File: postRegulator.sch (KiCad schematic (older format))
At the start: 18 parts

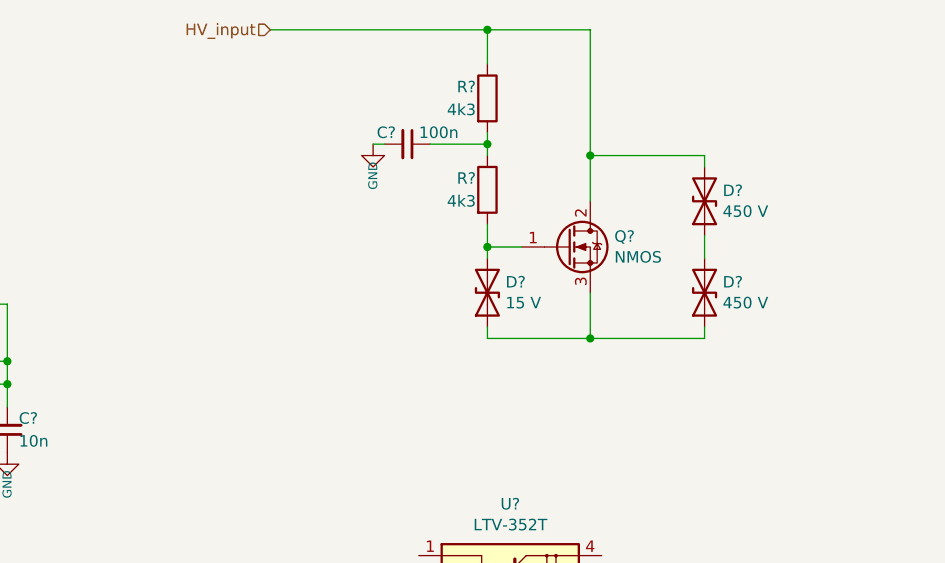
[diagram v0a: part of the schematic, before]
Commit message: - added DC/DC converter to library, - moved ammeter & drivers to sub-sheet, - further develop
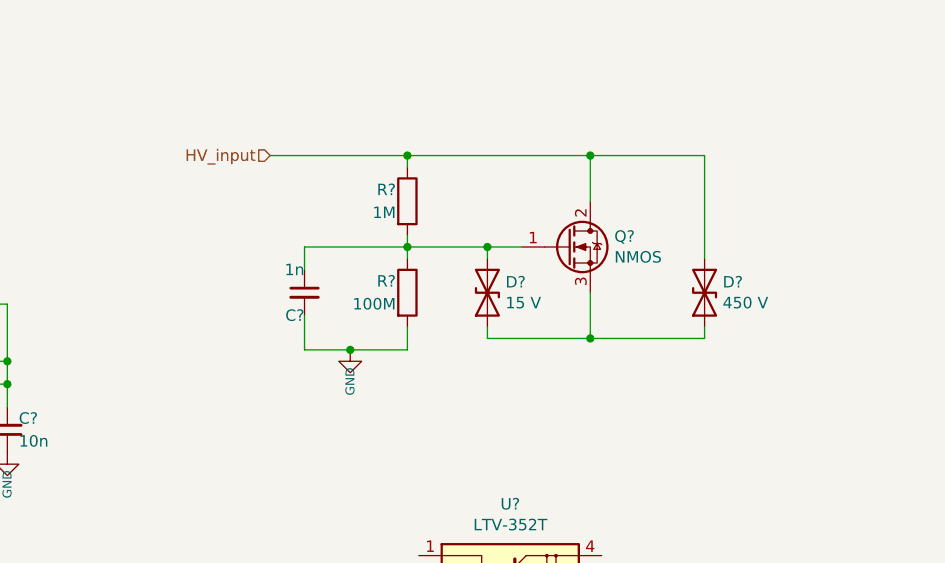
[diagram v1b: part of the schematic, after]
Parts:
- removed D?: 450 V, symbol Device:D_TVS
- C?: value 100n -> 1n
- R?: value 4k3 -> 100M
- R?: value 4k3 -> 1M
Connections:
- net GND: now also R?.2
- net at D?.2 (A2), Q?.1 (G): now also C?.1, R?.1, R?.2; no longer R?.2
- net at D?.1 (A1), Q?.3 (S): now also D?.1 (A1)
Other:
- moved on the sheet: C?, D?, R?
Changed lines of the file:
@@
 $Descr A4 11693 8268
 encoding utf-8
-Sheet 6 7
+Sheet 6 8
 Title ""
 Date ""
@@
 Wire Wire Line
 	3550 3700 3550 3650
-Text HLabel 2600 2350 0    50   Input ~ 0
+Text HLabel 2600 2900 0    50   Input ~ 0
 HV_input
-Wire Wire Line
-	2600 2350 3550 2350
-Wire Wire Line
-	4000 2350 4000 2900
 $Comp
 L Device:D_TVS D?
-U 1 1 5F4666BF
+U 1 1 5F466775
 P 4500 3500
 F 0 "D?" V 4546 3421 50  0000 R CNN
@@
 	0    -1   -1   0
 $EndComp
-$Comp
-L Device:D_TVS D?
-U 1 1 5F466775
-P 4500 3100
-F 0 "D?" V 4546 3021 50  0000 R CNN
-F 1 "450 V" V 4455 3021 50  0000 R CNN
-F 2 "" H 4500 3100 50  0001 C CNN
-F 3 "~" H 4500 3100 50  0001 C CNN
-	1    4500 3100
-	0    -1   -1   0
-$EndComp
 Wire Wire Line
 	4500 3650 4500 3700
@@
 Connection ~ 4000 3700
 Wire Wire Line
-	4500 3350 4500 3250
-Wire Wire Line
-	4500 2950 4500 2900
-Wire Wire Line
 	4500 2900 4000 2900
 Connection ~ 4000 2900
@@
 L Device:R R?
 U 1 1 5F46852F
-P 3550 3050
+P 3200 3500
 AR Path="/5F40DCB9/5F46852F" Ref="R?"  Part="1"
 AR Path="/5F463F4C/5F46852F" Ref="R?"  Part="1"
-F 0 "R?" H 3500 3100 50  0000 R CNN
-F 1 "4k3" H 3500 3000 50  0000 R CNN
-F 2 "" V 3480 3050 50  0001 C CNN
-F 3 "~" H 3550 3050 50  0001 C CNN
-	1    3550 3050
+F 0 "R?" H 3150 3550 50  0000 R CNN
+F 1 "100M" H 3150 3450 50  0000 R CNN
+F 2 "" V 3130 3500 50  0001 C CNN
+F 3 "~" H 3200 3500 50  0001 C CNN
+	1    3200 3500
 	1    0    0    -1
 $EndComp
@@
 L Device:R R?
 U 1 1 5F46860E
-P 3550 2650
+P 3200 3100
 AR Path="/5F40DCB9/5F46860E" Ref="R?"  Part="1"
 AR Path="/5F463F4C/5F46860E" Ref="R?"  Part="1"
-F 0 "R?" H 3500 2700 50  0000 R CNN
-F 1 "4k3" H 3500 2600 50  0000 R CNN
-F 2 "" V 3480 2650 50  0001 C CNN
-F 3 "~" H 3550 2650 50  0001 C CNN
-	1    3550 2650
-	1    0    0    -1
-$EndComp
-Wire Wire Line
-	3550 3200 3550 3300
-Connection ~ 3550 3300
-Connection ~ 3550 2350
-Wire Wire Line
-	3550 2350 4000 2350
-Wire Wire Line
-	3550 2500 3550 2350
-Wire Wire Line
-	3550 2800 3550 2850
+F 0 "R?" H 3150 3150 50  0000 R CNN
+F 1 "1M" H 3150 3050 50  0000 R CNN
+F 2 "" V 3130 3100 50  0001 C CNN
+F 3 "~" H 3200 3100 50  0001 C CNN
+	1    3200 3100
+	1    0    0    -1
+$EndComp
+Wire Wire Line
+	3200 3650 3200 3750
 $Comp
 L Device:C_Small C?
 U 1 1 5F469A6E
-P 3200 2850
+P 2750 3500
 AR Path="/5F40DCB9/5F469A6E" Ref="C?"  Part="1"
 AR Path="/5F463F4C/5F469A6E" Ref="C?"  Part="1"
-F 0 "C?" V 3150 2800 50  0000 R CNN
-F 1 "100n" V 3150 2900 50  0000 L CNN
-F 2 "" H 3200 2850 50  0001 C CNN
-F 3 "~" H 3200 2850 50  0001 C CNN
-	1    3200 2850
-	0    1    1    0
-$EndComp
-Wire Wire Line
-	3300 2850 3550 2850
-Connection ~ 3550 2850
-Wire Wire Line
-	3550 2850 3550 2900
+F 0 "C?" H 2750 3400 50  0000 R CNN
+F 1 "1n" H 2750 3600 50  0000 R CNN
+F 2 "" H 2750 3500 50  0001 C CNN
+F 3 "~" H 2750 3500 50  0001 C CNN
+	1    2750 3500
+	1    0    0    -1
+$EndComp
 $Comp
 L power:GND #PWR?
 U 1 1 5F46ABD8
-P 3050 2850
+P 2950 3750
 AR Path="/5F40DCB9/5F46ABD8" Ref="#PWR?"  Part="1"
 AR Path="/5F463F4C/5F46ABD8" Ref="#PWR?"  Part="1"
-F 0 "#PWR?" H 3050 2690 50  0001 C CNN
-F 1 "GND" V 3050 2773 39  0000 R CNN
-F 2 "" H 3050 2850 50  0001 C CNN
-F 3 "" H 3050 2850 50  0001 C CNN
-	1    3050 2850
-	1    0    0    -1
-$EndComp
-Wire Wire Line
-	3100 2850 3050 2850
+F 0 "#PWR?" H 2950 3590 50  0001 C CNN
+F 1 "GND" V 2950 3673 39  0000 R CNN
+F 2 "" H 2950 3750 50  0001 C CNN
+F 3 "" H 2950 3750 50  0001 C CNN
+	1    2950 3750
+	1    0    0    -1
+$EndComp
 $Comp
 L Device:C_Small C?
@@
 	1    0    0    -1
 $EndComp
+Wire Wire Line
+	3200 3250 3200 3300
+Connection ~ 3550 3300
+Connection ~ 3200 3300
+Wire Wire Line
+	3200 3300 3200 3350
+Wire Wire Line
+	2750 3400 2750 3300
+Wire Wire Line
+	2750 3750 2750 3600
+Wire Wire Line
+	3200 2950 3200 2900
+Wire Wire Line
+	3200 3300 3550 3300
+Wire Wire Line
+	3200 3300 2750 3300
+Connection ~ 3200 2900
+Wire Wire Line
+	3200 2900 4000 2900
+Wire Wire Line
+	2600 2900 3200 2900
+Wire Wire Line
+	3200 3750 2950 3750
+Connection ~ 2950 3750
+Wire Wire Line
+	2950 3750 2750 3750
+Wire Wire Line
+	4500 2900 4500 3350
 $EndSCHEMATC

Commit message: - changes..
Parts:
- removed C?: 1n, symbol Device:C_Small
- removed D?: 15 V, symbol Device:D_TVS
- removed D?: 450 V, symbol Device:D_TVS
- removed Q?: NMOS, symbol Device:Q_NMOS_GDS
- removed R?: 100M, symbol Device:R
- added C?: 10n 6 kV, symbol Device:C_Small
- added C? (x2): 1u, symbol Device:C_Small
- added C?: 9n9 12k5V, symbol Device:C_Small
- added C?: 346n, symbol Device:C_Small
- added C? (x2): 100n, symbol Device:C_Small
- added C?: 100p, symbol Device:C_Small
- added D? (x6): 1N4448, Diode_SMD:D_SOD-323_HandSoldering, symbol Device:D_Small
- added D? (x2): 1SS355, Diode_SMD:D_SOD-323_HandSoldering, symbol Device:D_Small
- added DMM: (10M), symbol Device:Voltmeter_DC
- added Liion? (x2): 4.0V, symbol Device:Battery_Cell
- added Load?, R_load: 17M, symbol Device:R
- added Q?: BC817, Package_TO_SOT_SMD:SOT-23, symbol Transistor_BJT:BC817
- added Q?: MMST3906, Package_TO_SOT_SMD:SOT-23, symbol Transistor_BJT:BC807
- added R? (x4): 100R, Resistor_SMD:R_0603_1608Metric_Pad1.05x0.95mm_HandSolder, symbol Device:R_Small
- added R?: 6M8, symbol Device:R_Small
- added R?: 3k3, Resistor_SMD:R_0603_1608Metric_Pad1.05x0.95mm_HandSolder, symbol Device:R_Small
- added R?: 68M, symbol Device:R
- added SW? (x2): SPDT, symbol Switch:SW_DPST_x2
- added TP?: TestPoint_Probe, symbol Connector:TestPoint_Probe
- added U10: LMC6482, symbol Amplifier_Operational:LMC6482
- added U?: F, Library_uScope:APD_P2_single, symbol uScope:APD_P2_single
- added U?: HVDC, Library_uScope:APD_P2_single, symbol uScope:APD_P2_single
- R?: value 1M -> 1k
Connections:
- net GND: now also C?.1, C?.1, C?.2, C?.2, D?.1 (K), D?.1 (K), D?.2 (A), D?.2 (A), DMM.1 (-), Liion?.1 (+), Liion?.2 (-), Load?.2, R_load.2, SW?.1 (A), U10.3 (+), U10.5 (+), U?.4 (-), U?.4 (-)
- net at R?.2: now also C?.2, SW?.2 (B)
- net HV_input: no longer names the net of R?.1
- net HV_input: now also D?.1 (K), D?.2 (A)
- new net: C?.1, R_load.1, U?.3 (+)
- new net: D?.1 (K), D?.2 (A) (x2)
- new net: C?.1, D?.1 (K), D?.1 (K)
- new net: C?.2, D?.2 (A), D?.2 (A)
- new net: C?.1, R?.1, U10.1
- new net: C?.2, R?.2, U10.2 (-)
- new net: C?.1, Load?.1, R?.1, U?.3 (+)
- new net: C?.1, C?.2, D?.1 (K), D?.2 (A), R?.1, R?.1, SW?.1 (A)
- new net: R?.1, SW?.2 (B)
- new net: C?.2, Q?.2 (E), Q?.2 (E), R?.2, R?.2, TP?.1
- new net: U10.6 (-), U10.7
- new net: C?.2, Q?.3 (C), R?.1, U10.4 (V-)
- new net: C?.1, Q?.3 (C), R?.1, U10.8 (V+)
- new net: Liion?.1 (+), R?.2
- new net: Liion?.2 (-), R?.2
- new net: Q?.1 (B), Q?.1 (B), R?.2
- new net: DMM.2 (+), R?.2
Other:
- note added: "@4 kV load 17 M: -4.7/+4.7V czyli ok. 12 Vpp ripple\n@6 kV load 17 M: -6.8/+6.8V czyli ok. 16 Vpp ripple\n\n@4 kV load 17 M 10n (fol.): -3.8/+3.8V czyli ok. 10 Vpp ripple\n@6 kV load 17 M 10n (fol.): -5.5/+5.5V czyli ok. 13.4 Vpp ripple\n\n@4 kV load 17 M 10n (fol.)+60n (cer.6kV): -/+4.1V czyli ok. Vpp ripple\n@6 kV load 17 M 10n (fol.)+60n (cer.6kV): -/+5.8V czyli ok. Vpp ripple"
- note added: "Uklad peak detector pomiar ripple"
- note added: "Uwaga: pomiar napiecia na jednej galezi, zawyza (doladowuje) druga.\nPo pomiarze jendej galezi trzeba zewrzec i na nowo naladowac uklad."
- moved on the sheet: Q?, R?, U?

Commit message: - W.i.P.
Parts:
- added U?: QSE159, OptoDevice:ONSemi_QSE15x, symbol Interface_Optical:QSE159
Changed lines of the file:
@@
 $Descr A4 11693 8268
 encoding utf-8
-Sheet 2 8
+Sheet 2 10
 Title ""
 Date ""
@@
 Wire Wire Line
 	8550 3650 8900 3650
+$Comp
+L Interface_Optical:QSE159 U?
+U 1 1 5F82FE36
+P 6400 5600
+F 0 "U?" H 6138 5646 50  0000 R CNN
+F 1 "QSE159" H 6138 5555 50  0000 R CNN
+F 2 "OptoDevice:ONSemi_QSE15x" H 6400 5200 50  0001 C CNN
+F 3 "http://www.onsemi.com/pub/Collateral/QSE159-D.pdf" H 7050 5900 50  0001 C CNN
+	1    6400 5600
+	1    0    0    -1
+$EndComp
 $EndSCHEMATC

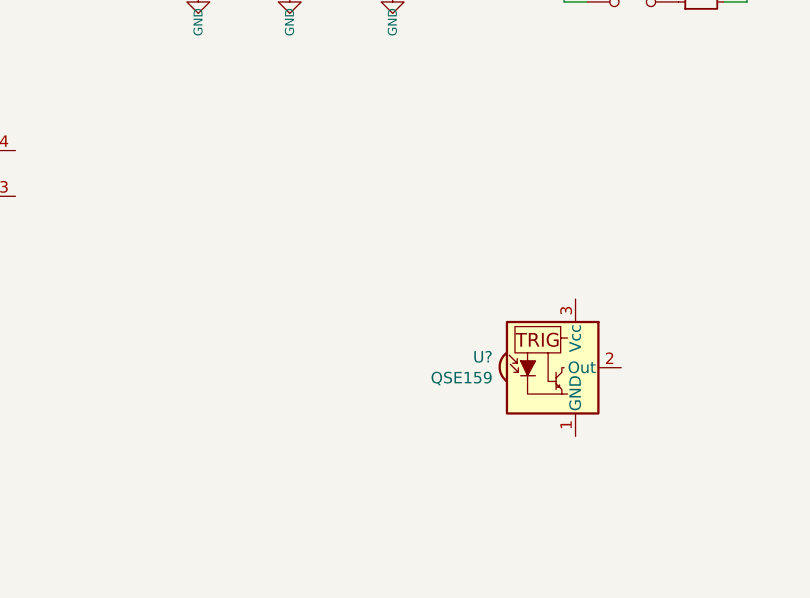
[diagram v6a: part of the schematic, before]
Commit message: - drivers modified - MCU replaced
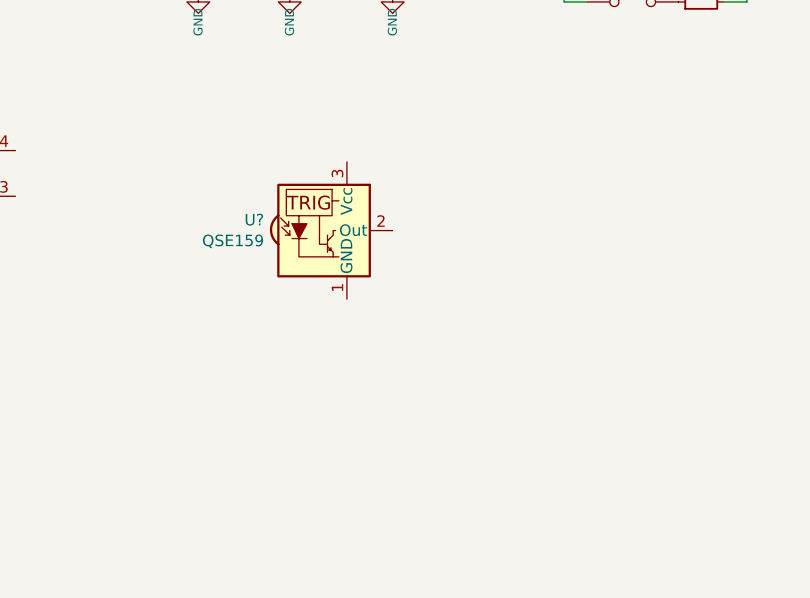
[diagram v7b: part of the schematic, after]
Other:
- moved on the sheet: U?
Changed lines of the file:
@@
 L Interface_Optical:QSE159 U?
 U 1 1 5F82FE36
-P 6400 5600
-F 0 "U?" H 6138 5646 50  0000 R CNN
-F 1 "QSE159" H 6138 5555 50  0000 R CNN
-F 2 "OptoDevice:ONSemi_QSE15x" H 6400 5200 50  0001 C CNN
-F 3 "http://www.onsemi.com/pub/Collateral/QSE159-D.pdf" H 7050 5900 50  0001 C CNN
-	1    6400 5600
+P 5400 5000
+F 0 "U?" H 5138 5046 50  0000 R CNN
+F 1 "QSE159" H 5138 4955 50  0000 R CNN
+F 2 "OptoDevice:ONSemi_QSE15x" H 5400 4600 50  0001 C CNN
+F 3 "http://www.onsemi.com/pub/Collateral/QSE159-D.pdf" H 6050 5300 50  0001 C CNN
+	1    5400 5000
 	1    0    0    -1
 $EndComp

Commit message: - high side (supply, MCU) - low side MCU - much small changes
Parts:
- removed U?: QSE159, OptoDevice:ONSemi_QSE15x, symbol Interface_Optical:QSE159
- C?: value 9n9 12k5V -> 1n5 6kV; footprint (none) -> Capacitor_THT:C_Rect_L26.5mm_W7.0mm_P22.50mm_MKS4
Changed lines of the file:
@@
 $Descr A4 11693 8268
 encoding utf-8
-Sheet 2 10
+Sheet 2 11
 Title ""
 Date ""
@@
 AR Path="/5F463F4C/5F6FE846" Ref="C?"  Part="1"
 F 0 "C?" V 5950 3050 50  0001 R CNN
-F 1 "9n9 12k5V" V 6000 3100 50  0000 C CNN
-F 2 "" H 5900 3100 50  0001 C CNN
+F 1 "1n5 6kV" V 6000 3100 50  0000 C CNN
+F 2 "Capacitor_THT:C_Rect_L26.5mm_W7.0mm_P22.50mm_MKS4" H 5900 3100 50  0001 C CNN
 F 3 "~" H 5900 3100 50  0001 C CNN
 	1    5900 3100
@@
 Wire Wire Line
 	8550 3650 8900 3650
-$Comp
-L Interface_Optical:QSE159 U?
-U 1 1 5F82FE36
-P 5400 5000
-F 0 "U?" H 5138 5046 50  0000 R CNN
-F 1 "QSE159" H 5138 4955 50  0000 R CNN
-F 2 "OptoDevice:ONSemi_QSE15x" H 5400 4600 50  0001 C CNN
-F 3 "http://www.onsemi.com/pub/Collateral/QSE159-D.pdf" H 6050 5300 50  0001 C CNN
-	1    5400 5000
-	1    0    0    -1
-$EndComp
 $EndSCHEMATC
